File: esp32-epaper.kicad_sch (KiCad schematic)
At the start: 49 parts, among them J1 USB-C 16P, J2 FPC-26P, Q1 AO3400A, SW1 SW SPDT, U1 ESP32-WROOM-32D, U2 SSD1680, U3 TP4056, U4 DW01A, U5 FS8205A, U6 HT7333-1

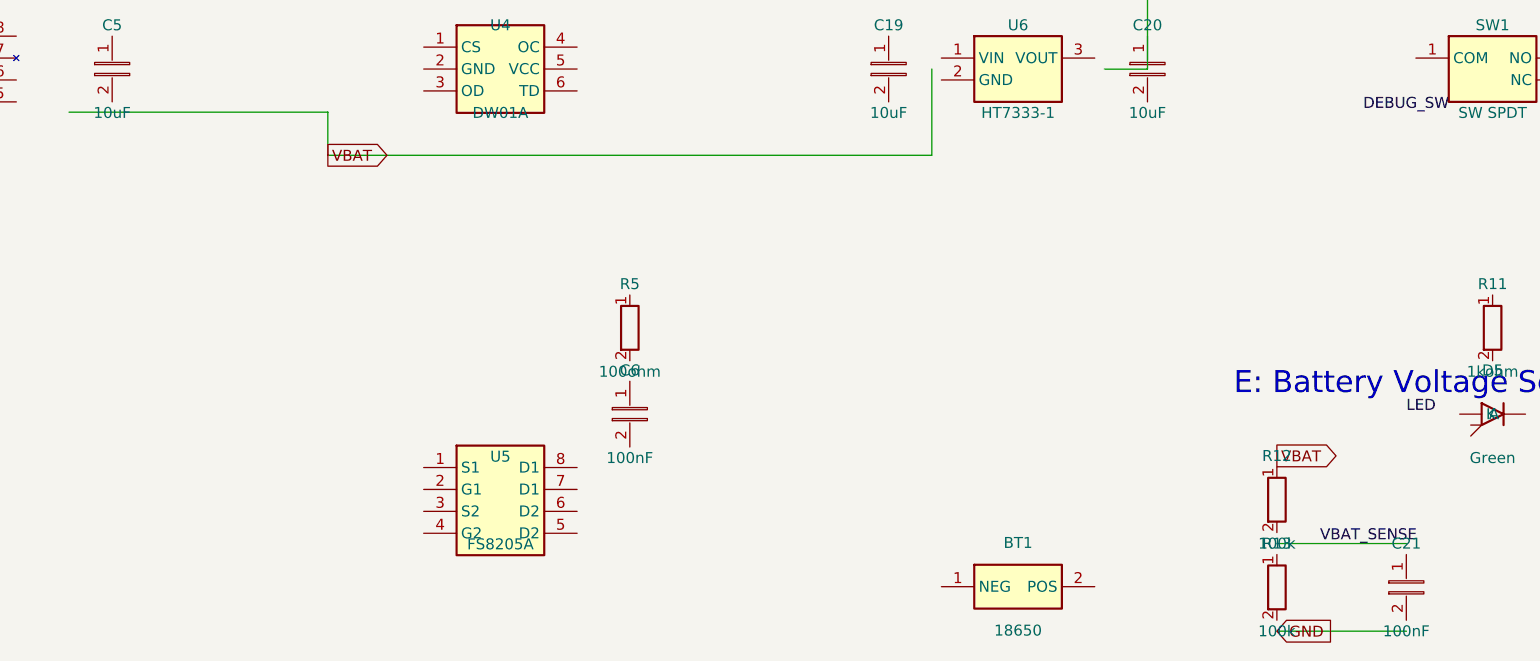
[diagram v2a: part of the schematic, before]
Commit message: feat: sync schematic with v1.1 power path requirements
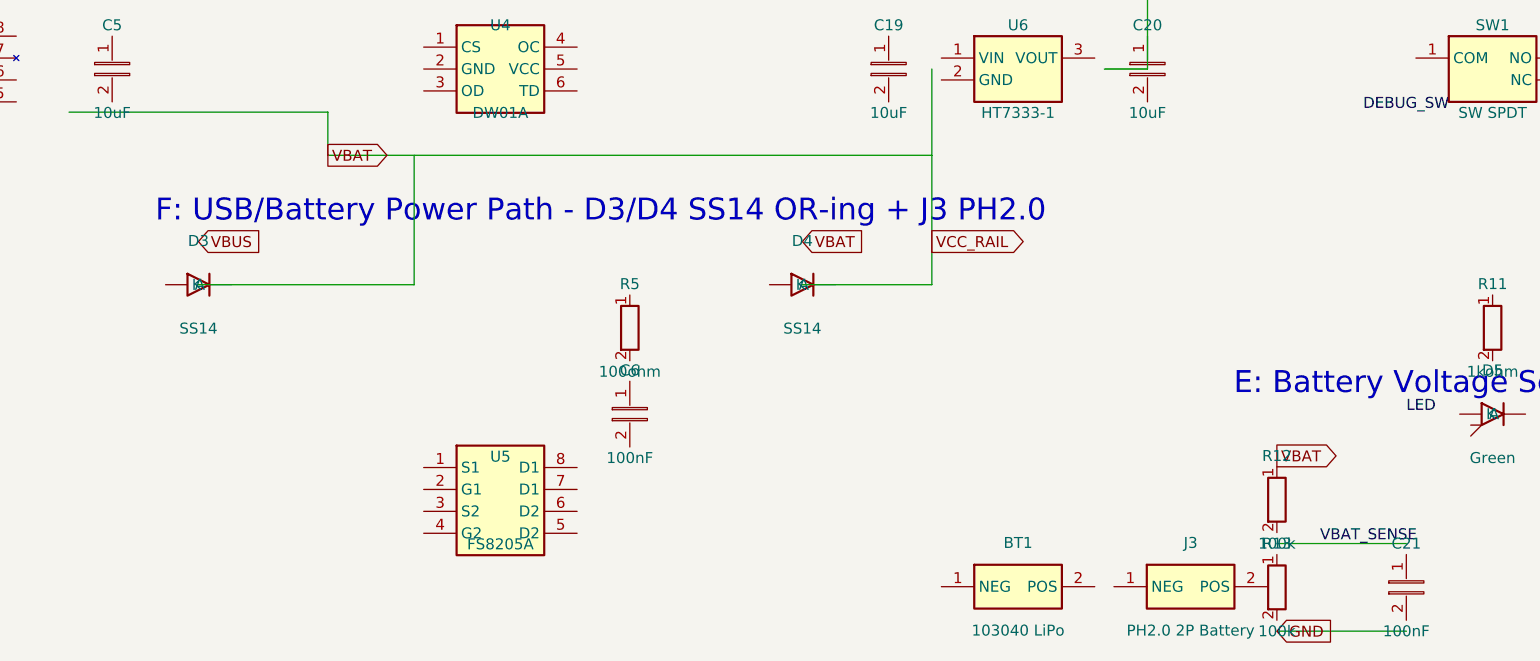
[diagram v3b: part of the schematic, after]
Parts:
- added D3, D4: SS14, Diode_SMD:D_SMA, symbol Device:D
- added J3: PH2.0 2P Battery, Connector_JST:JST_PH_B2B-PH-K_1x02_P2.00mm_Vertical, symbol esp32-epaper-lib:BatteryHolder_18650
- BT1: value 18650 -> 103040 LiPo
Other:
- note added: "F: USB/Battery Power Path - D3/D4 SS14 OR-ing + J3 PH2.0"
- title: ESP32 E-Paper Badge v1.0 -> ESP32 E-Paper Badge v1.1
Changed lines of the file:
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@@
   (paper "A3" portrait)
   (title_block
-    (title "ESP32 E-Paper Badge v1.0")
-    (date "2025-05-27")
-    (rev "1.0")
+    (title "ESP32 E-Paper Badge v1.1")
+    (date "2026-06-04")
+    (rev "1.1")
     (company "LuckyDog")
     (comment 1 "ESP32-WROOM-32D + SSD1680 + TP4056 + HT7333")
-    (comment 2 "2.13\" Tri-color E-Paper, USB-C Charging")
+    (comment 2 "2.13\" Tri-color E-Paper, USB-C Charging + USB Direct Power")
+  )
+  (text "F: USB/Battery Power Path - D3/D4 SS14 OR-ing + J3 PH2.0" (at 100 228 0)
+    (effects (font (size 2.54 2.54)) (justify left bottom))
   )
   (text "E: Battery Voltage Sensing (GPIO34)" (at 225 248 0)
@@
     (effects (font (size 2.54 2.54)) (justify left bottom))
   )
+  (wire (pts (xy 105 235) (xy 130 235))
+    (stroke (width 0) (type default))
+  )
+  (wire (pts (xy 175 235) (xy 190 235))
+    (stroke (width 0) (type default))
+  )
+  (wire (pts (xy 130 235) (xy 130 220))
+    (stroke (width 0) (type default))
+  )
+  (wire (pts (xy 190 235) (xy 190 220))
+    (stroke (width 0) (type default))
+  )
   (wire (pts (xy 230 265.0) (xy 245 265.0))
     (stroke (width 0) (type default))
@@
   (wire (pts (xy 40 10) (xy 40 20))
     (stroke (width 0) (type default))
+  )
+  (global_label "VBUS" (shape input) (at 105 230 0) (fields_autoplaced)
+    (effects (font (size 1.27 1.27)) (justify left))
+  )
+  (global_label "VBAT" (shape input) (at 175 230 0) (fields_autoplaced)
+    (effects (font (size 1.27 1.27)) (justify left))
+  )
+  (global_label "VCC_RAIL" (shape output) (at 190 230 0) (fields_autoplaced)
+    (effects (font (size 1.27 1.27)) (justify left))
   )
   (global_label "VBAT" (shape output) (at 230 254.84 0) (fields_autoplaced)
@@
       (effects (font (size 1.27 1.27)))
     )
-    (property "Value" "18650" (at 200 275.08 0)
+    (property "Value" "103040 LiPo" (at 200 275.08 0)
       (effects (font (size 1.27 1.27)))
     )
@@
         (path "/6281fcfa-6553-4706-b287-236232e6465c"
           (reference "C21") (unit 1)
+        )
+      )
+    )
+  )
+  (symbol (lib_id "Device:D") (at 105 235 0) (unit 1)
+    (in_bom yes) (on_board yes) (dnp no)
+    (property "Reference" "D3" (at 105 229.92 0)
+      (effects (font (size 1.27 1.27)))
+    )
+    (property "Value" "SS14" (at 105 240.08 0)
+      (effects (font (size 1.27 1.27)))
+    )
+    (property "Footprint" "Diode_SMD:D_SMA" (at 105 235 0)
+      (effects (font (size 1.27 1.27)) hide)
+    )
+    (pin "1")
+    (pin "2")
+    (instances
+      (project "esp32-epaper"
+        (path "/6281fcfa-6553-4706-b287-236232e6465c"
+          (reference "D3") (unit 1)
+        )
+      )
+    )
+  )
+  (symbol (lib_id "Device:D") (at 175 235 0) (unit 1)
+    (in_bom yes) (on_board yes) (dnp no)
+    (property "Reference" "D4" (at 175 229.92 0)
+      (effects (font (size 1.27 1.27)))
+    )
+    (property "Value" "SS14" (at 175 240.08 0)
+      (effects (font (size 1.27 1.27)))
+    )
+    (property "Footprint" "Diode_SMD:D_SMA" (at 175 235 0)
+      (effects (font (size 1.27 1.27)) hide)
+    )
+    (pin "1")
+    (pin "2")
+    (instances
+      (project "esp32-epaper"
+        (path "/6281fcfa-6553-4706-b287-236232e6465c"
+          (reference "D4") (unit 1)
+        )
+      )
+    )
+  )
+  (symbol (lib_id "esp32-epaper-lib:BatteryHolder_18650") (at 220 270 0) (unit 1)
+    (in_bom yes) (on_board yes) (dnp no)
+    (property "Reference" "J3" (at 220 264.92 0)
+      (effects (font (size 1.27 1.27)))
+    )
+    (property "Value" "PH2.0 2P Battery" (at 220 275.08 0)
+      (effects (font (size 1.27 1.27)))
+    )
+    (property "Footprint" "Connector_JST:JST_PH_B2B-PH-K_1x02_P2.00mm_Vertical" (at 220 270 0)
+      (effects (font (size 1.27 1.27)) hide)
+    )
+    (pin "1")
+    (pin "2")
+    (instances
+      (project "esp32-epaper"
+        (path "/6281fcfa-6553-4706-b287-236232e6465c"
+          (reference "J3") (unit 1)
         )
       )
@@
   )
   (symbol_instances
+    (path "/6281fcfa-6553-4706-b287-236232e6465c/53e737b7-03c0-4868-9fe6-27c0dd3b17c9" (reference "D3") (unit 1) (value "SS14") (footprint "Diode_SMD:D_SMA"))
+    (path "/6281fcfa-6553-4706-b287-236232e6465c/88836973-5578-4160-8428-95954fbaeb1b" (reference "D4") (unit 1) (value "SS14") (footprint "Diode_SMD:D_SMA"))
+    (path "/6281fcfa-6553-4706-b287-236232e6465c/20d072a2-3c48-4913-bd50-65fec731faf1" (reference "J3") (unit 1) (value "PH2.0 2P Battery") (footprint "Connector_JST:JST_PH_B2B-PH-K_1x02_P2.00mm_Vertical"))
     (path "/6281fcfa-6553-4706-b287-236232e6465c/54a7cd7b-874f-4a66-ba55-5686449b3f6c" (reference "R12") (unit 1) (value "100k") (footprint ""))
     (path "/6281fcfa-6553-4706-b287-236232e6465c/06daef87-462d-45ee-8b88-b0b52aab98b7" (reference "R13") (unit 1) (value "100k") (footprint ""))
@@
     (path "/6281fcfa-6553-4706-b287-236232e6465c/6e4178a8-5b19-43ac-9226-53bc6ba6a0b0" (reference "C19") (unit 1) (value "10uF") (footprint ""))
     (path "/6281fcfa-6553-4706-b287-236232e6465c/f1fd58d5-7561-4f1f-bbb4-68c23dcbb0c4" (reference "C20") (unit 1) (value "10uF") (footprint ""))
-    (path "/6281fcfa-6553-4706-b287-236232e6465c/56aca0fc-4e1e-4d14-8bc5-37386bf2f76f" (reference "BT1") (unit 1) (value "18650") (footprint ""))
+    (path "/6281fcfa-6553-4706-b287-236232e6465c/56aca0fc-4e1e-4d14-8bc5-37386bf2f76f" (reference "BT1") (unit 1) (value "103040 LiPo") (footprint ""))
     (path "/6281fcfa-6553-4706-b287-236232e6465c/a6c1ee91-081a-48b5-b354-80b019599a76" (reference "SW1") (unit 1) (value "SW SPDT") (footprint ""))
     (path "/6281fcfa-6553-4706-b287-236232e6465c/ef915b23-cd38-459e-98a6-52f5482c4f7d" (reference "D5") (unit 1) (value "Green") (footprint ""))
